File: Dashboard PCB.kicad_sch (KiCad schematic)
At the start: 36 parts, among them J1 Controls_Leader_Export_02x06, J2 Supp_01x02, J4 FAN_CTRL_01x02, J5 Horn_In_01x02, J6 Horn_Out_01x02

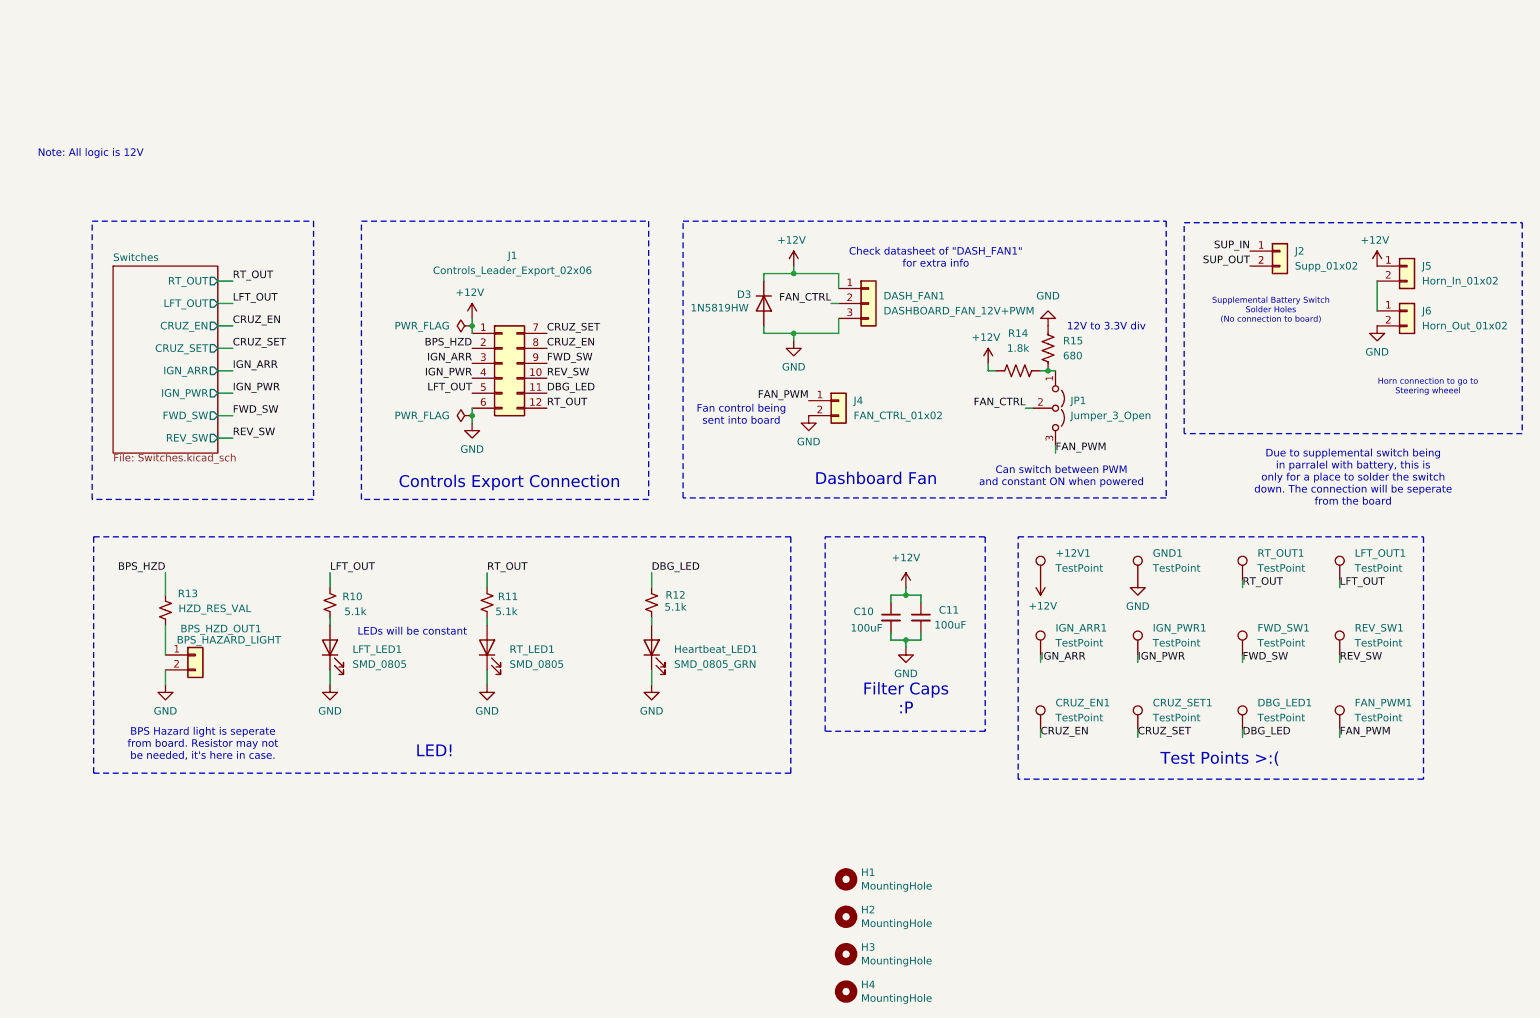
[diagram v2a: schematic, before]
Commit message: Footprint all assigned, and updated to PCB
Ready for a check in to make sure everything is looking alright
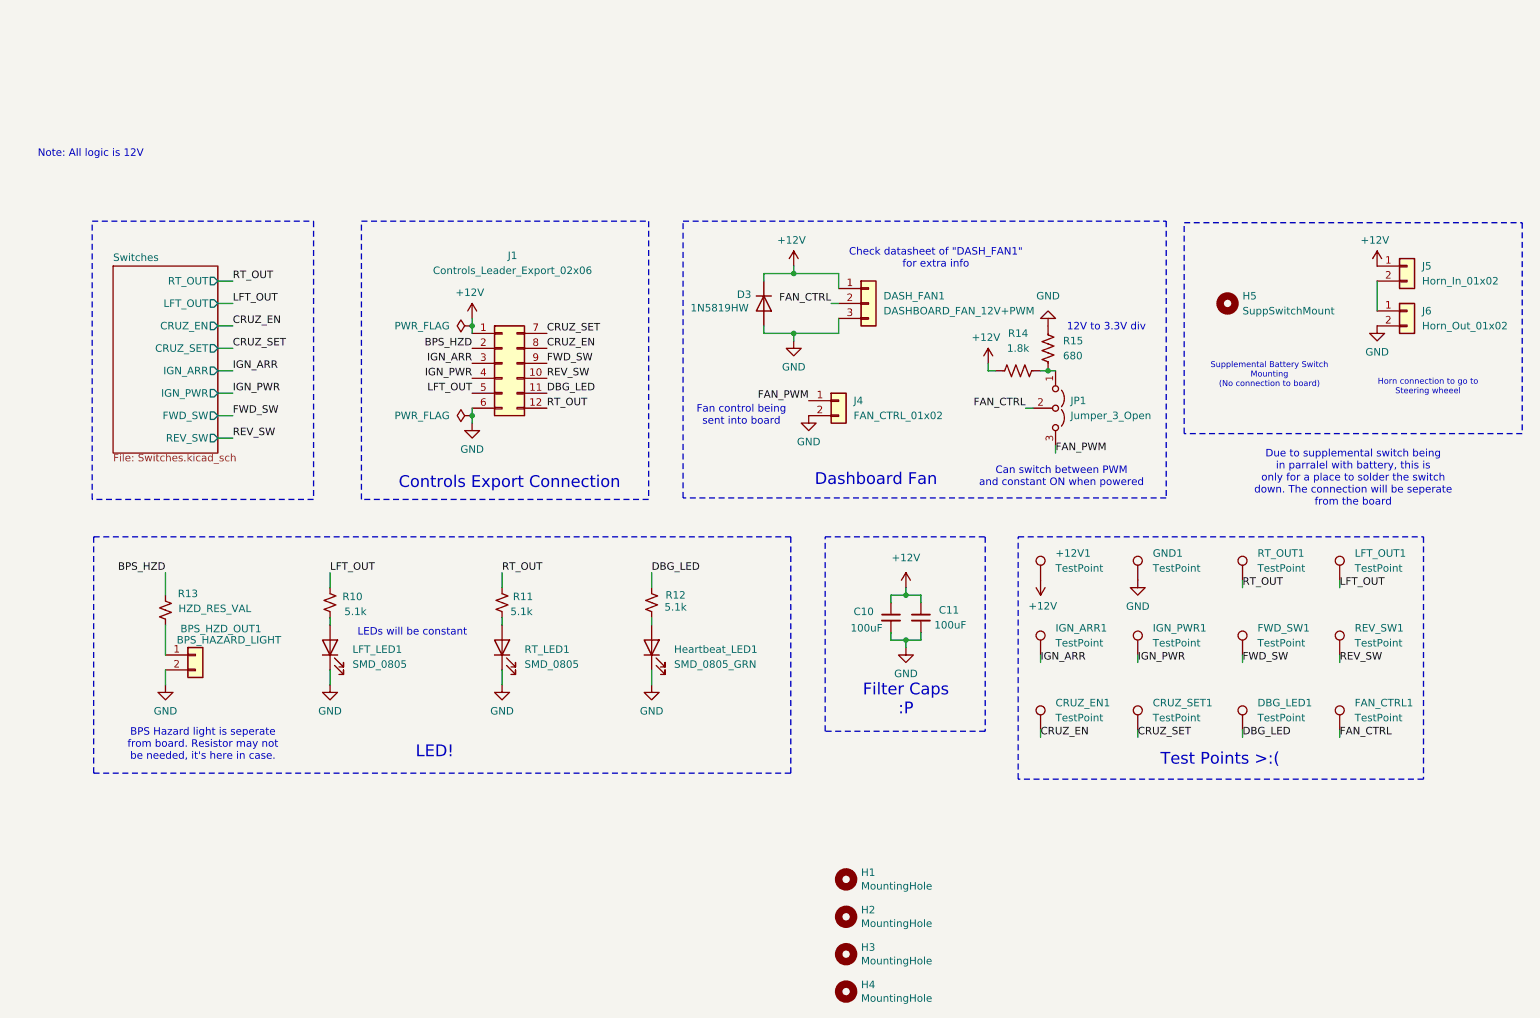
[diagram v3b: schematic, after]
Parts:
- removed J2: Supp_01x02, symbol Connector_Generic:Conn_01x02
- added H5: SuppSwitchMount, switched:Supp_Switch, symbol Mechanical:MountingHole
- +12V1, CRUZ_EN1, CRUZ_SET1, DBG_LED1, FWD_SW1, GND1, IGN_ARR1, IGN_PWR1, LFT_OUT1, REV_SW1, RT_OUT1: footprint TestPoint:TestPoint_Plated_Hole_D3.0mm -> Connector_PinHeader_2.54mm:PinHeader_1x01_P2.54mm_Vertical
- FAN_CTRL1: renamed from FAN_PWM1; footprint TestPoint:TestPoint_Plated_Hole_D3.0mm -> Connector_PinHeader_2.54mm:PinHeader_1x01_P2.54mm_Vertical
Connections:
- net FAN_CTRL: now also FAN_CTRL1.1
- net FAN_PWM: no longer FAN_CTRL1.1
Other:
- note added: "Supplemental Battery Switch Mounting (No connection to board)"
- note removed: "Supplemental Battery Switch Solder Holes (No connection to board)"
- moved on the sheet: R11, RT_LED1
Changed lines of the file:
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@@
 	(wire
 		(pts
-			(xy 97.79 128.27) (xy 97.79 129.54)
+			(xy 100.33 128.27) (xy 100.33 129.54)
 		)
 		(stroke
@@
 	(wire
 		(pts
-			(xy 97.79 139.7) (xy 97.79 137.16)
+			(xy 100.33 139.7) (xy 100.33 137.16)
 		)
 		(stroke
@@
 	(wire
 		(pts
-			(xy 97.79 123.19) (xy 97.79 120.65)
+			(xy 100.33 123.19) (xy 100.33 120.65)
 		)
 		(stroke
@@
 		)
 	)
-	(text "Supplemental Battery Switch\nSolder Holes\n(No connection to board)"
+	(text "Supplemental Battery Switch\nMounting\n(No connection to board)"
 		(exclude_from_sim no)
-		(at 230.886 76.2 0)
+		(at 230.632 87.122 0)
 		(effects
 			(font
@@
 		)
 	)
-	(label "FAN_PWM"
-		(at 242.57 148.59 0)
-		(fields_autoplaced yes)
-		(effects
-			(font
-				(size 1.27 1.27)
-			)
-			(justify left bottom)
-		)
-	)
 	(label "LFT_OUT"
 		(at 242.57 123.19 0)
@@
 		)
 	)
-	(label "SUP_IN"
-		(at 227.33 66.04 180)
-		(fields_autoplaced yes)
-		(effects
-			(font
-				(size 1.27 1.27)
-			)
-			(justify right bottom)
-		)
-	)
 	(label "FWD_SW"
 		(at 226.06 135.89 0)
@@
 		)
 	)
-	(label "SUP_OUT"
-		(at 227.33 68.58 180)
+	(label "FAN_CTRL"
+		(at 242.57 148.59 0)
 		(fields_autoplaced yes)
 		(effects
@@
 				(size 1.27 1.27)
 			)
-			(justify right bottom)
+			(justify left bottom)
 		)
 	)
@@
 	)
 	(label "RT_OUT"
-		(at 97.79 120.65 0)
+		(at 100.33 120.65 0)
 		(fields_autoplaced yes)
 		(effects
@@
 			)
 		)
-		(property "Footprint" "TestPoint:TestPoint_Plated_Hole_D3.0mm"
+		(property "Footprint" "Connector_PinHeader_2.54mm:PinHeader_1x01_P2.54mm_Vertical"
 			(at 213.36 121.92 0)
 			(effects
@@
 	(symbol
 		(lib_id "Device:LED")
-		(at 97.79 133.35 90)
+		(at 100.33 133.35 90)
 		(unit 1)
 		(exclude_from_sim no)
@@
 		(fields_autoplaced yes)
 		(property "Reference" "RT_LED1"
-			(at 101.6 133.6674 90)
+			(at 104.14 133.6674 90)
 			(effects
 				(font
@@
 		)
 		(property "Value" "SMD_0805"
-			(at 101.6 136.2074 90)
+			(at 104.14 136.2074 90)
 			(effects
 				(font
@@
 		)
 		(property "Footprint" "LED_SMD:LED_0805_2012Metric"
-			(at 97.79 133.35 0)
+			(at 100.33 133.35 0)
 			(effects
 				(font
@@
 		)
 		(property "Datasheet" "~"
-			(at 97.79 133.35 0)
+			(at 100.33 133.35 0)
 			(effects
 				(font
@@
 		)
 		(property "Description" "Light emitting diode"
-			(at 97.79 133.35 0)
+			(at 100.33 133.35 0)
 			(effects
 				(font
@@
 			)
 		)
-		(property "Footprint" "TestPoint:TestPoint_Plated_Hole_D3.0mm"
+		(property "Footprint" "Connector_PinHeader_2.54mm:PinHeader_1x01_P2.54mm_Vertical"
 			(at 247.65 134.62 0)
 			(effects
@@
 	(symbol
 		(lib_id "power:GND")
-		(at 97.79 139.7 0)
+		(at 100.33 139.7 0)
 		(unit 1)
 		(exclude_from_sim no)
@@
 		(fields_autoplaced yes)
 		(property "Reference" "#PWR010"
-			(at 97.79 146.05 0)
+			(at 100.33 146.05 0)
 			(effects
 				(font
@@
 		)
 		(property "Value" "GND"
-			(at 97.79 144.145 0)
+			(at 100.33 144.145 0)
 			(effects
 				(font
@@
 		)
 		(property "Footprint" ""
-			(at 97.79 139.7 0)
+			(at 100.33 139.7 0)
 			(effects
 				(font
@@
 		)
 		(property "Datasheet" ""
-			(at 97.79 139.7 0)
+			(at 100.33 139.7 0)
 			(effects
 				(font
@@
 		)
 		(property "Description" "Power symbol creates a global label with name \"GND\" , ground"
-			(at 97.79 139.7 0)
+			(at 100.33 139.7 0)
 			(effects
 				(font
@@
 	)
 	(symbol
-		(lib_id "Connector_Generic:Conn_01x02")
-		(at 232.41 66.04 0)
-		(unit 1)
-		(exclude_from_sim no)
-		(in_bom yes)
-		(on_board yes)
-		(dnp no)
-		(fields_autoplaced yes)
-		(property "Reference" "J2"
-			(at 234.95 66.0399 0)
-			(effects
-				(font
-					(size 1.27 1.27)
-				)
-				(justify left)
-			)
-		)
-		(property "Value" "Supp_01x02"
-			(at 234.95 68.5799 0)
-			(effects
-				(font
-					(size 1.27 1.27)
-				)
-				(justify left)
-			)
-		)
-		(property "Footprint" ""
-			(at 232.41 66.04 0)
-			(effects
-				(font
-					(size 1.27 1.27)
-				)
-				(hide yes)
-			)
-		)
-		(property "Datasheet" "~"
-			(at 232.41 66.04 0)
-			(effects
-				(font
-					(size 1.27 1.27)
-				)
-				(hide yes)
-			)
-		)
-		(property "Description" "Generic connector, single row, 01x02, script generated (kicad-library-utils/schlib/autogen/connector/)"
-			(at 232.41 66.04 0)
-			(effects
-				(font
-					(size 1.27 1.27)
-				)
-				(hide yes)
-			)
-		)
-		(pin "1"
-		)
-		(pin "2"
-		)
-		(instances
-			(project ""
-				(path "/db66d699-14af-49af-adc9-07d31d38aebd"
-					(reference "J2")
-					(unit 1)
-				)
-			)
-		)
-	)
-	(symbol
 		(lib_id "Connector:TestPoint")
 		(at 191.77 147.32 0)
@@
 			)
 		)
-		(property "Footprint" "TestPoint:TestPoint_Plated_Hole_D3.0mm"
+		(property "Footprint" "Connector_PinHeader_2.54mm:PinHeader_1x01_P2.54mm_Vertical"
 			(at 196.85 147.32 0)
 			(effects
@@
 			)
 		)
-		(property "Footprint" "TestPoint:TestPoint_Plated_Hole_D3.0mm"
+		(property "Footprint" "Connector_PinHeader_2.54mm:PinHeader_1x01_P2.54mm_Vertical"
 			(at 231.14 147.32 0)
 			(effects
@@
 			)
 		)
-		(property "Footprint" "TestPoint:TestPoint_Plated_Hole_D3.0mm"
+		(property "Footprint" "Connector_PinHeader_2.54mm:PinHeader_1x01_P2.54mm_Vertical"
 			(at 213.36 147.32 0)
 			(effects
@@
 			)
 		)
-		(property "Footprint" "TestPoint:TestPoint_Plated_Hole_D3.0mm"
+		(property "Footprint" "Connector_PinHeader_2.54mm:PinHeader_1x01_P2.54mm_Vertical"
 			(at 196.85 121.92 0)
 			(effects
@@
 			)
 		)
-		(property "Footprint" "TestPoint:TestPoint_Plated_Hole_D3.0mm"
+		(property "Footprint" "Connector_PinHeader_2.54mm:PinHeader_1x01_P2.54mm_Vertical"
 			(at 196.85 134.62 0)
 			(effects
@@
 	)
 	(symbol
+		(lib_id "Mechanical:MountingHole")
+		(at 223.52 74.93 0)
+		(unit 1)
+		(exclude_from_sim yes)
+		(in_bom no)
+		(on_board yes)
+		(dnp no)
+		(fields_autoplaced yes)
+		(property "Reference" "H5"
+			(at 226.06 73.6599 0)
+			(effects
+				(font
+					(size 1.27 1.27)
+				)
+				(justify left)
+			)
+		)
+		(property "Value" "SuppSwitchMount"
+			(at 226.06 76.1999 0)
+			(effects
+				(font
+					(size 1.27 1.27)
+				)
+				(justify left)
+			)
+		)
+		(property "Footprint" "switched:Supp_Switch"
+			(at 223.52 74.93 0)
+			(effects
+				(font
+					(size 1.27 1.27)
+				)
+				(hide yes)
+			)
+		)
+		(property "Datasheet" "~"
+			(at 223.52 74.93 0)
+			(effects
+				(font
+					(size 1.27 1.27)
+				)
+				(hide yes)
+			)
+		)
+		(property "Description" "Mounting Hole without connection"
+			(at 223.52 74.93 0)
+			(effects
+				(font
+					(size 1.27 1.27)
+				)
+				(hide yes)
+			)
+		)
+		(instances
+			(project ""
+				(path "/db66d699-14af-49af-adc9-07d31d38aebd"
+					(reference "H5")
+					(unit 1)
+				)
+			)
+		)
+	)
+	(symbol
 		(lib_id "Device:R_Small_US")
-		(at 97.79 125.73 0)
+		(at 100.33 125.73 0)
 		(unit 1)
 		(exclude_from_sim no)
@@
 		(dnp no)
 		(property "Reference" "R11"
-			(at 101.346 124.714 0)
+			(at 103.886 124.714 0)
 			(effects
 				(font
@@
 		)
 		(property "Value" "5.1k"
-			(at 101.092 127.254 0)
+			(at 103.632 127.254 0)
 			(effects
 				(font
@@
 		)
 		(property "Footprint" "Resistor_SMD:R_0805_2012Metric"
-			(at 97.79 125.73 0)
+			(at 100.33 125.73 0)
 			(effects
 				(font
@@
 		)
 		(property "Datasheet" "~"
-			(at 97.79 125.73 0)
+			(at 100.33 125.73 0)
 			(effects
 				(font
@@
 		)
 		(property "Description" "Resistor, small US symbol"
-			(at 97.79 125.73 0)
+			(at 100.33 125.73 0)
 			(effects
 				(font
@@
 		)
 		(property "P/N" "CRCW0805100RFKEAHP"
-			(at 97.79 125.73 90)
+			(at 100.33 125.73 90)
 			(effects
 				(font
@@
 			)
 		)
-		(property "Footprint" "TestPoint:TestPoint_Plated_Hole_D3.0mm"
+		(property "Footprint" "Connector_PinHeader_2.54mm:PinHeader_1x01_P2.54mm_Vertical"
 			(at 213.36 134.62 0)
 			(effects
@@
 			)
 		)
-		(property "Footprint" "TestPoint:TestPoint_Plated_Hole_D3.0mm"
+		(property "Footprint" "Connector_PinHeader_2.54mm:PinHeader_1x01_P2.54mm_Vertical"
 			(at 247.65 121.92 0)
 			(effects
@@
 		(dnp no)
 		(fields_autoplaced yes)
-		(property "Reference" "FAN_PWM1"
+		(property "Reference" "FAN_CTRL1"
 			(at 245.11 142.7479 0)
 			(effects
@@
 			)
 		)
-		(property "Footprint" "TestPoint:TestPoint_Plated_Hole_D3.0mm"
+		(property "Footprint" "Connector_PinHeader_2.54mm:PinHeader_1x01_P2.54mm_Vertical"
 			(at 247.65 147.32 0)
 			(effects
@@
 			(project "Dashboard PCB"
 				(path "/db66d699-14af-49af-adc9-07d31d38aebd"
-					(reference "FAN_PWM1")
+					(reference "FAN_CTRL1")
 					(unit 1)
 				)
@@
 			)
 		)
-		(property "Footprint" "TestPoint:TestPoint_Plated_Hole_D3.0mm"
+		(property "Footprint" "Connector_PinHeader_2.54mm:PinHeader_1x01_P2.54mm_Vertical"
 			(at 231.14 121.92 0)
 			(effects
@@
 			)
 		)
-		(property "Footprint" "TestPoint:TestPoint_Plated_Hole_D3.0mm"
+		(property "Footprint" "Connector_PinHeader_2.54mm:PinHeader_1x01_P2.54mm_Vertical"
 			(at 231.14 134.62 0)
 			(effects
